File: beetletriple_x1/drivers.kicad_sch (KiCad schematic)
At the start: 24 parts, among them J2 motor_out, J3 motor_out, J4 motor_out, Q1 IRF8313PBF, Q2 IRF8313PBF, Q3 IRF8313PBF, Q4 IRF8313PBF, Q5 IRF8313PBF, Q6 IRF8313PBF, U11 NCP81155MN, U12 NCP81155MN, U13 NCP81155MN, U14 NCP81155MN, U15 NCP81155MN, U16 NCP81155MN

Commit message: Beetletriple version x1 with the dfn-8 gate driver finally fix up routing and errors
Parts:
- U11, U12, U13, U14, U15, U16: LCSC (none) -> C173765
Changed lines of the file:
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@@
+      (effects (font (size 1.27 1.27)) hide)
+    )
+    (property "LCSC" "C173765" (id 4) (at 46.99 51.435 0)
       (effects (font (size 1.27 1.27)) hide)
     )
@@
       (effects (font (size 1.27 1.27)) hide)
     )
+    (property "LCSC" "C173765" (id 4) (at 46.99 110.49 0)
+      (effects (font (size 1.27 1.27)) hide)
+    )
     (pin "1")
     (pin "2")
@@
     )
     (property "Datasheet" "" (id 3) (at 46.99 170.18 0)
+      (effects (font (size 1.27 1.27)) hide)
+    )
+    (property "LCSC" "C173765" (id 4) (at 46.99 170.18 0)
       (effects (font (size 1.27 1.27)) hide)
     )
@@
       (effects (font (size 1.27 1.27)) hide)
     )
+    (property "LCSC" "C173765" (id 4) (at 93.98 62.865 0)
+      (effects (font (size 1.27 1.27)) hide)
+    )
     (pin "1")
     (pin "2")
@@
     )
     (property "Datasheet" "" (id 3) (at 93.98 121.92 0)
+      (effects (font (size 1.27 1.27)) hide)
+    )
+    (property "LCSC" "C173765" (id 4) (at 93.98 121.92 0)
       (effects (font (size 1.27 1.27)) hide)
     )
@@
       (effects (font (size 1.27 1.27)) hide)
     )
+    (property "LCSC" "C173765" (id 4) (at 93.98 181.61 0)
+      (effects (font (size 1.27 1.27)) hide)
+    )

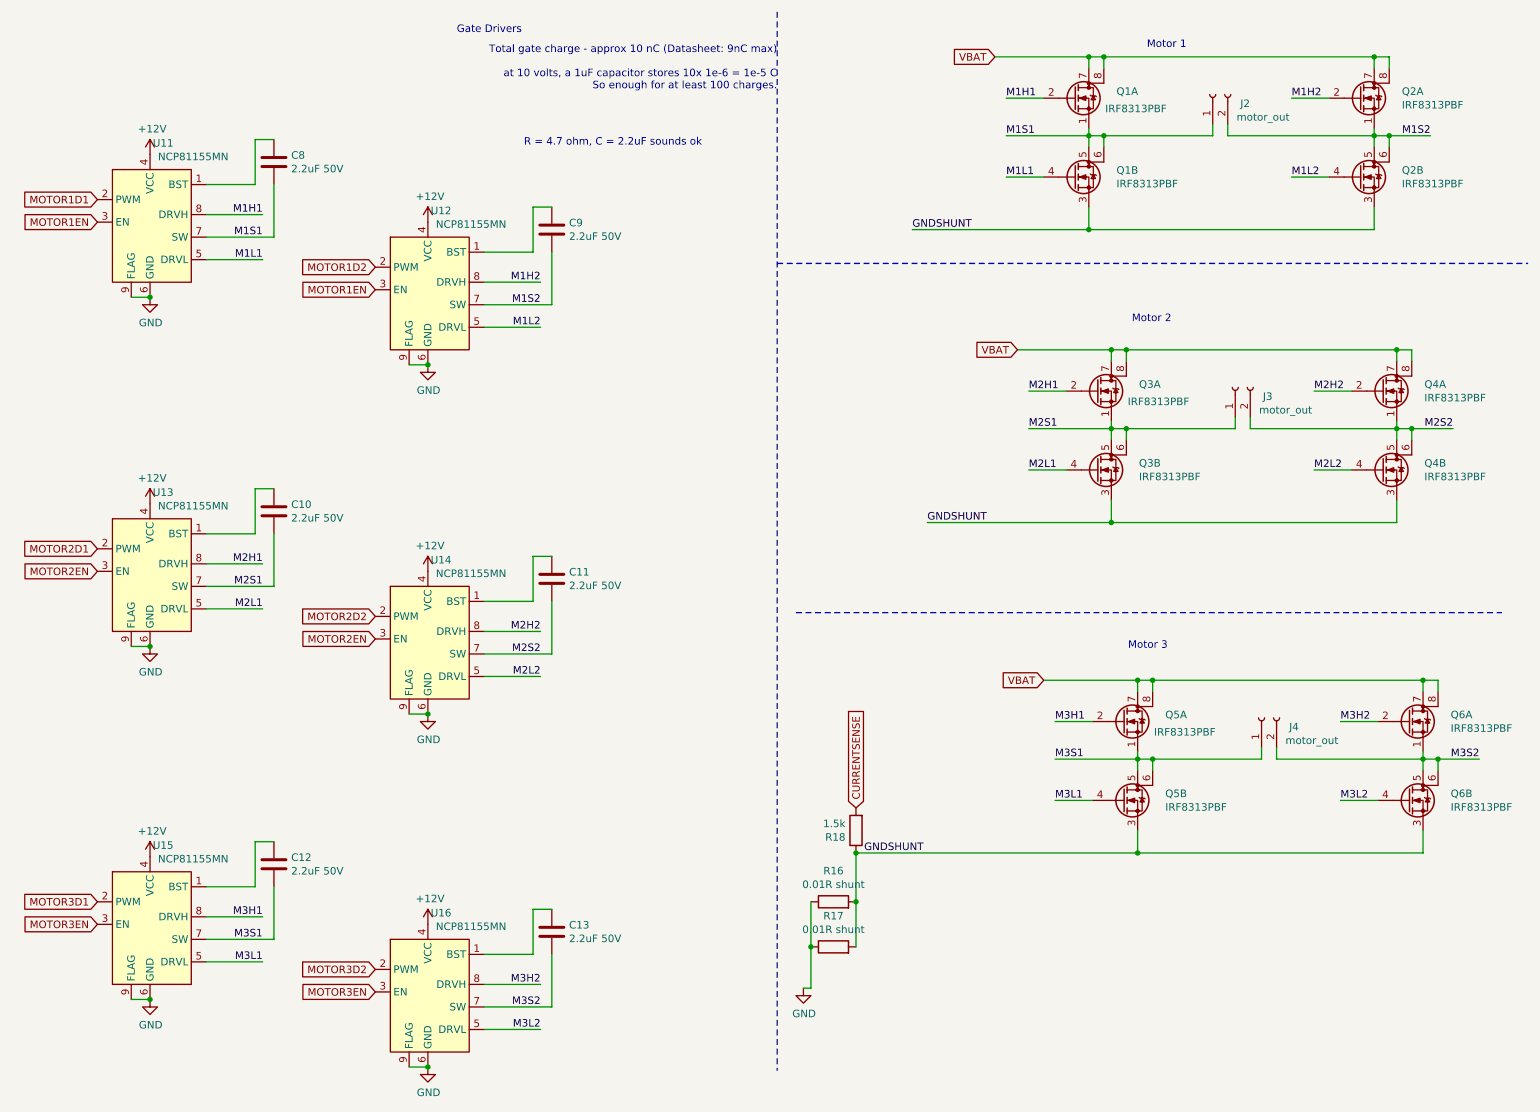
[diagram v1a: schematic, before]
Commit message: Add gate resistors; re-layout
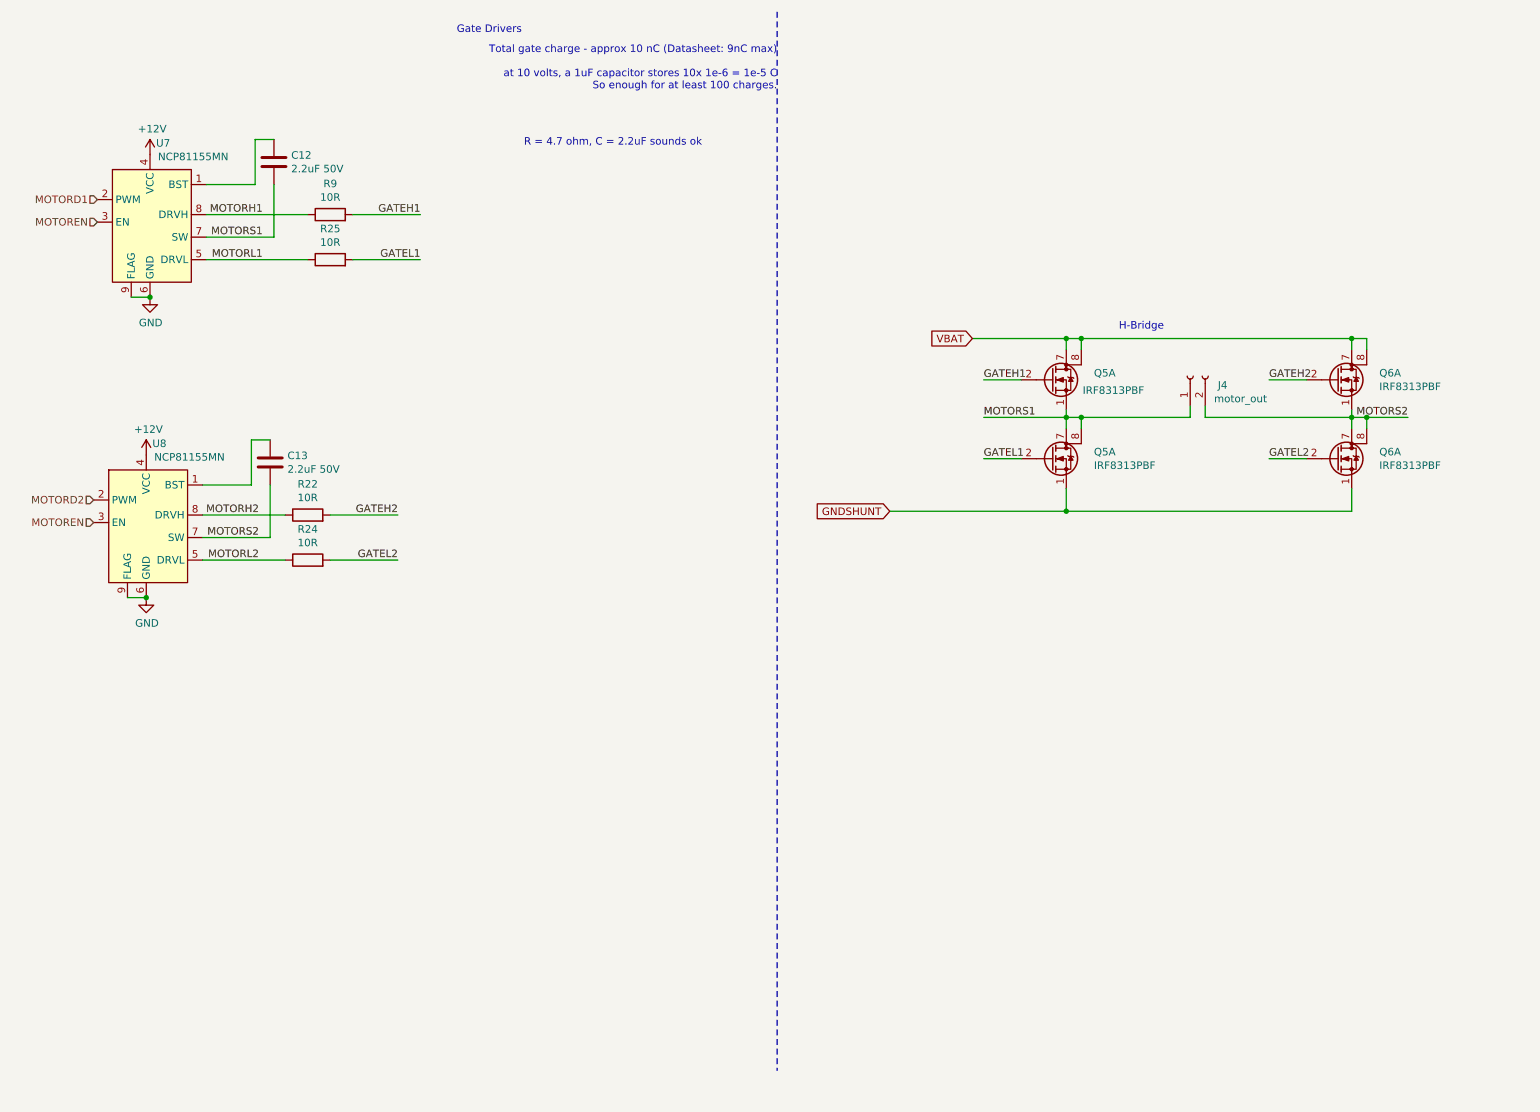
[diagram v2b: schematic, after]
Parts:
- removed C10, C11, C12, C13: 2.2uF 50V, Capacitor_SMD:C_1206_3216Metric, symbol Device:C
- removed J3, J4: motor_out, beetletriple:TerminalBlock_motor, symbol Connector:Conn_01x02_Female
- removed Q3, Q4, Q5, Q6: IRF8313PBF, Package_SO:SOIC-8_3.9x4.9mm_P1.27mm, symbol beetletriple:Q_Dual_NMOS_S1G1S2G2D2D2D1D1
- removed R16, R17: 0.01R shunt, Resistor_SMD:R_2512_6332Metric_Pad1.40x3.35mm_HandSolder, symbol Device:R
- removed R18: 1.5k, Resistor_SMD:R_0805_2012Metric, symbol Device:R
- removed U13, U14, U15, U16: NCP81155MN, Package_DFN_QFN:DFN-8-1EP_3x3mm_P0.5mm_EP1.66x2.38mm, symbol beetletriple:NCP81155MN
- added R22, R24, R25, R9: 10R, Resistor_SMD:R_0805_2012Metric, symbol Device:R
- renumbered C8 to C12, C9 to C13, J2 to J4, Q1 to Q5, Q2 to Q6, U11 to U7, U12 to U8
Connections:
- net GNDSHUNT: now also Q5.1 (S), Q6.1 (S); no longer Q5.3 (S), Q6.3 (S)
- net M1H1 renamed GATEH1
- net GATEH1: now also R9.2; no longer U7.8 (DRVH)
- net M1H2 renamed GATEH2
- net GATEH2: now also R22.2; no longer U8.8 (DRVH)
- net M1L1 renamed MOTORL1
- net MOTORL1: now also R25.1; no longer Q5.4 (G)
- net M1L2 renamed MOTORL2
- net MOTORL2: now also R24.1; no longer Q6.4 (G)
- net M1S1 renamed MOTORS1
- net MOTORS1: now also Q5.7 (D), Q5.8 (D); no longer Q5.5 (D), Q5.6 (D)
- net M1S2 renamed MOTORS2
- net MOTORS2: now also Q6.7 (D), Q6.8 (D); no longer Q6.5 (D), Q6.6 (D)
- net MOTOR1D1 renamed MOTORD1
- net MOTOR1D2 renamed MOTORD2
- net MOTOR1EN renamed MOTOREN
- new net GATEL1: Q5.2 (G), R25.2
- new net GATEL2: Q6.2 (G), R24.2
- new net MOTORH1: R9.1, U7.8 (DRVH)
- new net MOTORH2: R22.1, U8.8 (DRVH)
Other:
- note added: "H-Bridge"
- note removed: "Motor 1"
- note removed: "Motor 2"
- note removed: "Motor 3"
- moved on the sheet: C13, J4, Q5A, Q6A, U8

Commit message: Footprints shenanigans
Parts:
- U7, U8: value NCP81155MN -> NCP81155MNTXG; footprint Package_DFN_QFN:DFN-8-1EP_3x3mm_P0.5mm_EP1.66x2.38mm -> beetletriple:DFN-8-3x3mm_hand1
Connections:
- net GATEH1 renamed TESTH1
- net GATEL1 renamed TESTL1
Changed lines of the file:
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@@
     (stroke (width 0) (type solid) (color 0 0 0 0))
   )
-  (wire (pts (xy 81.28 47.625) (xy 92.71 47.625))
-    (stroke (width 0) (type solid) (color 0 0 0 0))
-  )
-  (wire (pts (xy 81.28 55.245) (xy 92.71 55.245))
+  (wire (pts (xy 81.28 47.625) (xy 95.885 47.625))
+    (stroke (width 0) (type solid) (color 0 0 0 0))
+  )
+  (wire (pts (xy 81.28 55.245) (xy 102.235 55.245))
+    (stroke (width 0) (type solid) (color 0 0 0 0))
+  )
+  (wire (pts (xy 95.885 43.815) (xy 95.885 47.625))
+    (stroke (width 0) (type solid) (color 0 0 0 0))
+  )
+  (wire (pts (xy 102.235 53.34) (xy 102.235 55.245))
     (stroke (width 0) (type solid) (color 0 0 0 0))
   )
@@
   (hierarchical_label "MOTOREN" (shape input) (at 38.1 48.895 180)
     (effects (font (size 1.27 1.27)) (justify right))
+  )
+  (hierarchical_label "TESTH1" (shape input) (at 95.885 43.815 90)
+    (effects (font (size 1.27 1.27)) (justify left))
+  )
+  (hierarchical_label "TESTL1" (shape input) (at 102.235 53.34 90)
+    (effects (font (size 1.27 1.27)) (justify left))
   )
   (symbol (lib_id "power:+12V") (at 46.355 88.265 0)
@@
     (in_bom yes) (on_board yes)
     (property "Reference" "U8" (id 0) (at 48.578 86.341 0))
-    (property "Value" "NCP81155MN" (id 1) (at 53.6575 88.6395 0))
-    (property "Footprint" "Package_DFN_QFN:DFN-8-1EP_3x3mm_P0.5mm_EP1.66x2.38mm" (id 2) (at 46.355 102.235 0)
+    (property "Value" "NCP81155MNTXG" (id 1) (at 54.9275 88.6395 0))
+    (property "Footprint" "beetletriple:DFN-8-3x3mm_hand1" (id 2) (at 46.355 102.235 0)
       (effects (font (size 1.27 1.27)) hide)
     )
@@
     (in_bom yes) (on_board yes)
     (property "Reference" "U7" (id 0) (at 49.212 35.541 0))
-    (property "Value" "NCP81155MN" (id 1) (at 54.2925 37.8395 0))
-    (property "Footprint" "Package_DFN_QFN:DFN-8-1EP_3x3mm_P0.5mm_EP1.66x2.38mm" (id 2) (at 46.99 51.435 0)
-      (effects (font (size 1.27 1.27)) hide)
-    )
+    (property "Value" "NCP81155MNTXG" (id 1) (at 55.5625 37.8395 0))
+    (property "Footprint" "beetletriple:DFN-8-3x3mm_hand1" (id 2) (at 46.99 51.435 0)
+      (effects (font (size 1.27 1.27)) hide)
+    )
